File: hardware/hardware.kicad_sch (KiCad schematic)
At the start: 0 parts

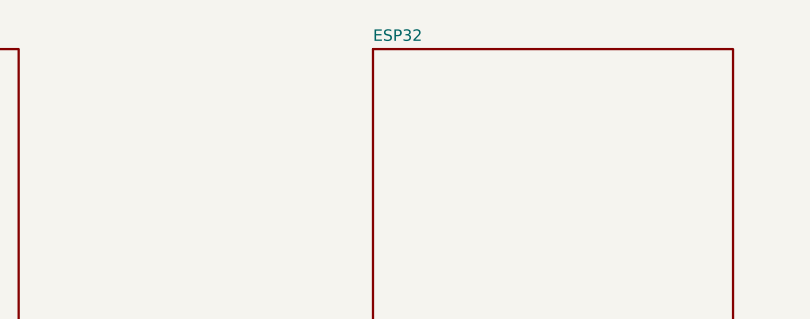
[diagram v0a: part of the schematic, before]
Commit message: Updated schematic to add STM32
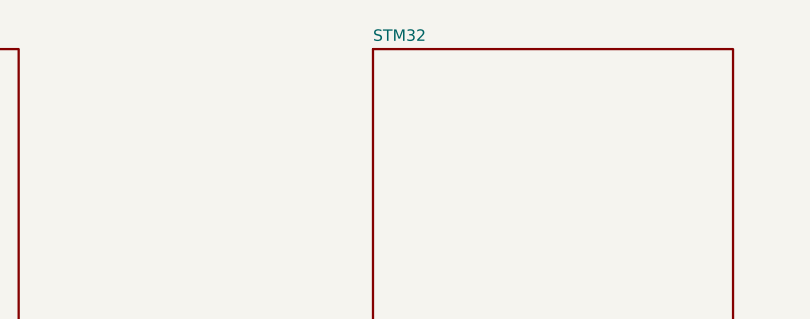
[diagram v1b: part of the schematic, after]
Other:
- sheet ESP32 renamed STM32
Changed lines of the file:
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@@
 			(color 0 132 0 0.3294117647)
 		)
-		(property "Sheetname" "ESP32"
+		(property "Sheetname" "STM32"
 			(at 134.62 68.4526 0)
 			(show_name no)

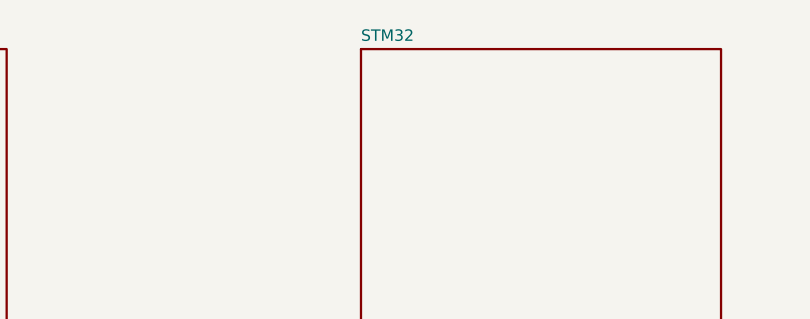
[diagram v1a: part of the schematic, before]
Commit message: Abstracted STM32 into it's own schematic block and settled boot mode and reset scheme
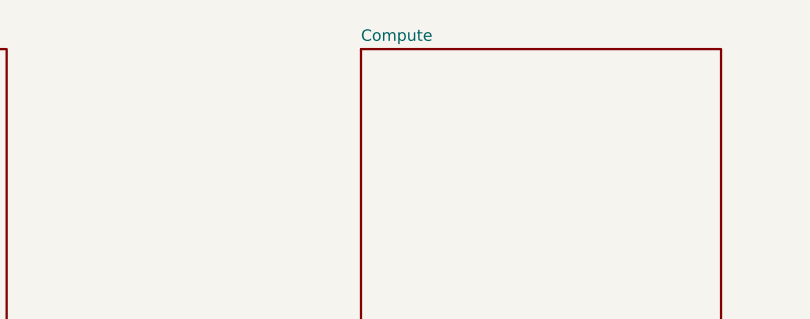
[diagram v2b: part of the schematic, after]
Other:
- sheet STM32 renamed Compute
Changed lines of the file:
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@@
 			(color 0 132 0 0.3294117647)
 		)
-		(property "Sheetname" "STM32"
+		(property "Sheetname" "Compute"
 			(at 134.62 68.4526 0)
 			(show_name no)

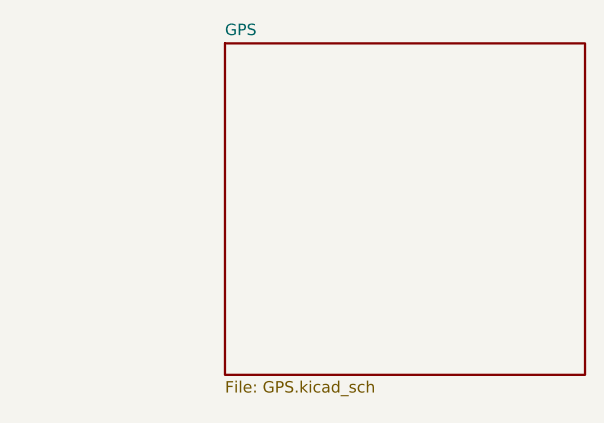
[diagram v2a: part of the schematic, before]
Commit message: Deleted GPS schematic to fit in compute sheet
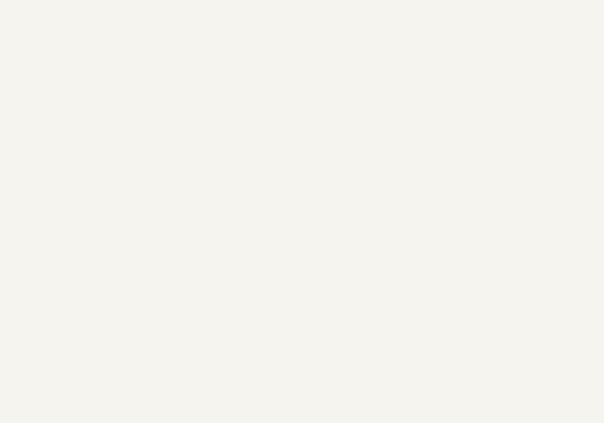
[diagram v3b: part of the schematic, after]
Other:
- removed sheet GPS
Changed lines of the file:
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@@
-		)
-	)
-	(sheet
-		(at 213.995 68.58)
-		(size 40.005 36.83)
-		(exclude_from_sim no)
-		(in_bom yes)
-		(on_board yes)
-		(dnp no)
-		(fields_autoplaced yes)
-		(stroke
-			(width 0.254)
-			(type solid)
-		)
-		(fill
-			(color 194 0 194 0.3294117647)
-		)
-		(property "Sheetname" "GPS"
-			(at 213.995 67.8176 0)
-			(show_name no)
-			(do_not_autoplace no)
-			(effects
-				(font
-					(size 1.27 1.27)
-				)
-				(justify left bottom)
-			)
-		)
-		(property "Sheetfile" "GPS.kicad_sch"
-			(at 213.995 106.0454 0)
-			(show_name no)
-			(do_not_autoplace no)
-			(effects
-				(font
-					(size 1.27 1.27)
-				)
-				(justify left top)
-			)
-		)
-		(instances
-			(project "hardware"
-				(path "/a19f636f-b28d-4c43-b96a-b02383edd3eb"
-					(page "6")
-				)
-			)
 		)
 	)

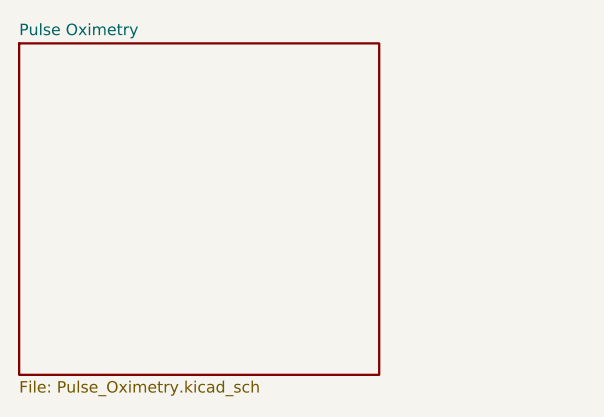
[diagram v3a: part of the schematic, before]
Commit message: Added PPG schematic page
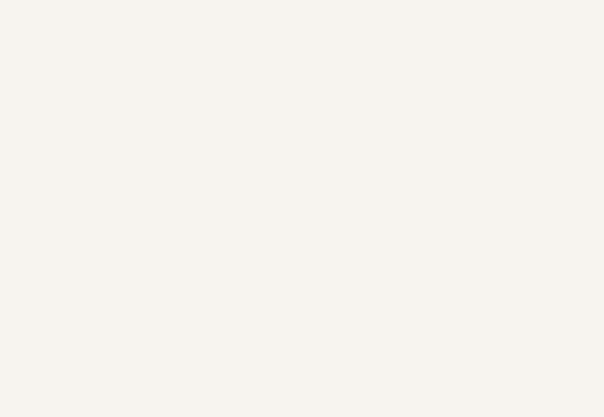
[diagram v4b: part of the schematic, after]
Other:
- removed sheet Pulse Oximetry
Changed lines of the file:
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@@
 	(paper "A4")
-	(sheet
-		(at 55.245 69.215)
-		(size 40.005 36.83)
-		(exclude_from_sim no)
-		(in_bom yes)
-		(on_board yes)
-		(dnp no)
-		(fields_autoplaced yes)
-		(stroke
-			(width 0.254)
-			(type solid)
-		)
-		(fill
-			(color 0 132 132 0.3294117647)
-		)
-		(property "Sheetname" "Pulse Oximetry"
-			(at 55.245 68.4526 0)
-			(show_name no)
-			(do_not_autoplace no)
-			(effects
-				(font
-					(size 1.27 1.27)
-				)
-				(justify left bottom)
-			)
-		)
-		(property "Sheetfile" "Pulse_Oximetry.kicad_sch"
-			(at 55.245 106.6804 0)
-			(show_name no)
-			(do_not_autoplace no)
-			(effects
-				(font
-					(size 1.27 1.27)
-				)
-				(justify left top)
-			)
-		)
-		(instances
-			(project "hardware"
-				(path "/a19f636f-b28d-4c43-b96a-b02383edd3eb"
-					(page "5")
-				)
-			)
-		)
-	)
 	(sheet
 		(at 134.62 69.215)

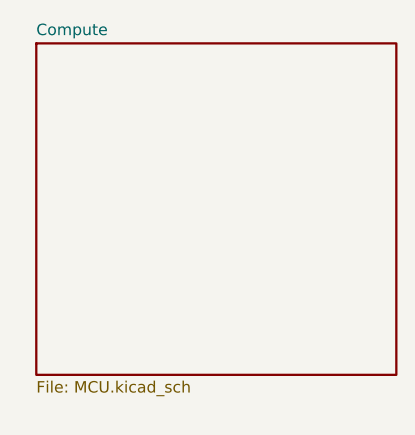
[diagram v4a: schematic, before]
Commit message: Added IMU and barometer, and connected to STM32
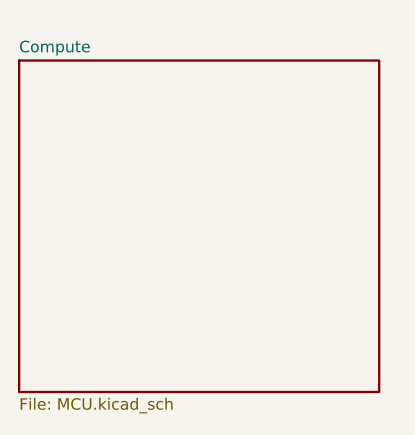
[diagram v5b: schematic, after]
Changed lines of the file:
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@@
 	(paper "A4")
 	(sheet
-		(at 134.62 69.215)
+		(at 132.715 71.12)
 		(size 40.005 36.83)
 		(exclude_from_sim no)
@@
 		)
 		(property "Sheetname" "Compute"
-			(at 134.62 68.4526 0)
+			(at 132.715 70.3576 0)
 			(show_name no)
 			(do_not_autoplace no)
@@
 		)
 		(property "Sheetfile" "MCU.kicad_sch"
-			(at 134.62 106.6804 0)
+			(at 132.715 108.5854 0)
 			(show_name no)
 			(do_not_autoplace no)
